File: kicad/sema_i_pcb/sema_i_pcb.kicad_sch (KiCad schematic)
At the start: 22 parts, among them SW1 SW_SPDT, SW2 SW_Push, U1 PIC24FJ64GA002-I_SP, U2 ESP8266-01_ESP-01, U3 edge_connector

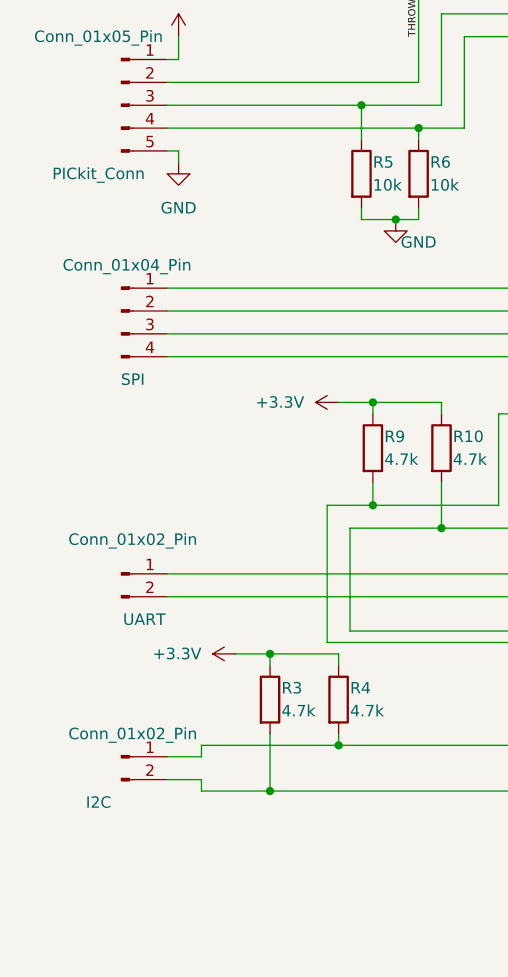
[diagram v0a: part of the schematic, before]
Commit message: Issue #9 : Kreiranje simbola i modela za Edge Connector
- Izmjenjen footprint edge connector-a
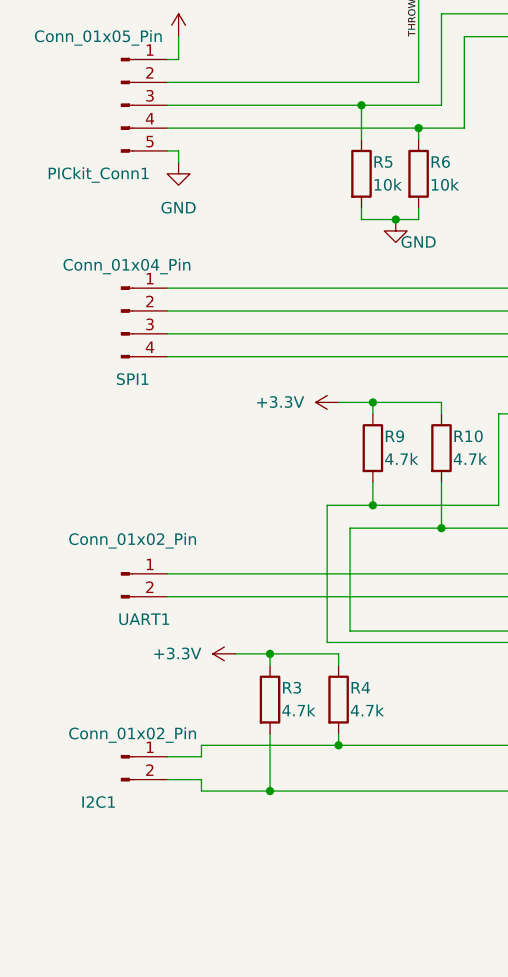
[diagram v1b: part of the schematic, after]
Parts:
- renumbered I2C to I2C1, PICkit_Conn to PICkit_Conn1, SPI to SPI1, UART to UART1
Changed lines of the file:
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@@
       (effects (font (size 1.27 1.27)) hide)
     )
+    (pin "1")
     (pin "10")
+    (pin "11")
+    (pin "12")
+    (pin "13")
+    (pin "14")
+    (pin "15")
+    (pin "16")
+    (pin "17")
+    (pin "18")
     (pin "19")
+    (pin "2")
+    (pin "20")
     (pin "21")
-    (pin "15")
+    (pin "22")
+    (pin "23")
     (pin "24")
-    (pin "13")
-    (pin "18")
-    (pin "11")
-    (pin "14")
+    (pin "25")
+    (pin "3")
+    (pin "4")
+    (pin "5")
+    (pin "6")
     (pin "7")
-    (pin "6")
     (pin "8")
-    (pin "16")
-    (pin "3")
-    (pin "12")
-    (pin "23")
-    (pin "2")
     (pin "9")
-    (pin "1")
-    (pin "25")
-    (pin "4")
-    (pin "22")
-    (pin "20")
-    (pin "17")
-    (pin "5")
     (instances
       (project "sema_i_pcb"
@@
   (symbol (lib_id "Connector:Conn_01x02_Pin") (at 24.13 132.08 0) (unit 1)
     (in_bom yes) (on_board yes) (dnp no)
-    (property "Reference" "UART" (at 26.67 137.16 0)
+    (property "Reference" "UART1" (at 26.67 137.16 0)
       (effects (font (size 1.27 1.27)))
     )
@@
       (project "sema_i_pcb"
         (path "/8dfcb1b3-4805-4434-ac9b-60b4afd3c281"
-          (reference "UART") (unit 1)
+          (reference "UART1") (unit 1)
         )
       )
@@
   (symbol (lib_id "Connector:Conn_01x04_Pin") (at 24.13 102.87 0) (unit 1)
     (in_bom yes) (on_board yes) (dnp no)
-    (property "Reference" "SPI" (at 25.4 110.49 0)
+    (property "Reference" "SPI1" (at 25.4 110.49 0)
       (effects (font (size 1.27 1.27)))
     )
@@
       (project "sema_i_pcb"
         (path "/8dfcb1b3-4805-4434-ac9b-60b4afd3c281"
-          (reference "SPI") (unit 1)
+          (reference "SPI1") (unit 1)
         )
       )
@@
   (symbol (lib_id "Connector:Conn_01x02_Pin") (at 24.13 152.4 0) (unit 1)
     (in_bom yes) (on_board yes) (dnp no)
-    (property "Reference" "I2C" (at 21.59 157.48 0)
+    (property "Reference" "I2C1" (at 21.59 157.48 0)
       (effects (font (size 1.27 1.27)))
     )
@@
       (project "sema_i_pcb"
         (path "/8dfcb1b3-4805-4434-ac9b-60b4afd3c281"
-          (reference "I2C") (unit 1)
+          (reference "I2C1") (unit 1)
         )
       )
@@
   (symbol (lib_id "Connector:Conn_01x05_Pin") (at 24.13 80.01 0) (unit 1)
     (in_bom yes) (on_board yes) (dnp no)
-    (property "Reference" "PICkit_Conn" (at 21.59 87.63 0)
+    (property "Reference" "PICkit_Conn1" (at 21.59 87.63 0)
       (effects (font (size 1.27 1.27)))
     )
@@
       (project "sema_i_pcb"
         (path "/8dfcb1b3-4805-4434-ac9b-60b4afd3c281"
-          (reference "PICkit_Conn") (unit 1)
-        )
-      )
+          (reference "PICkit_Conn1") (unit 1)
+        )
+      )

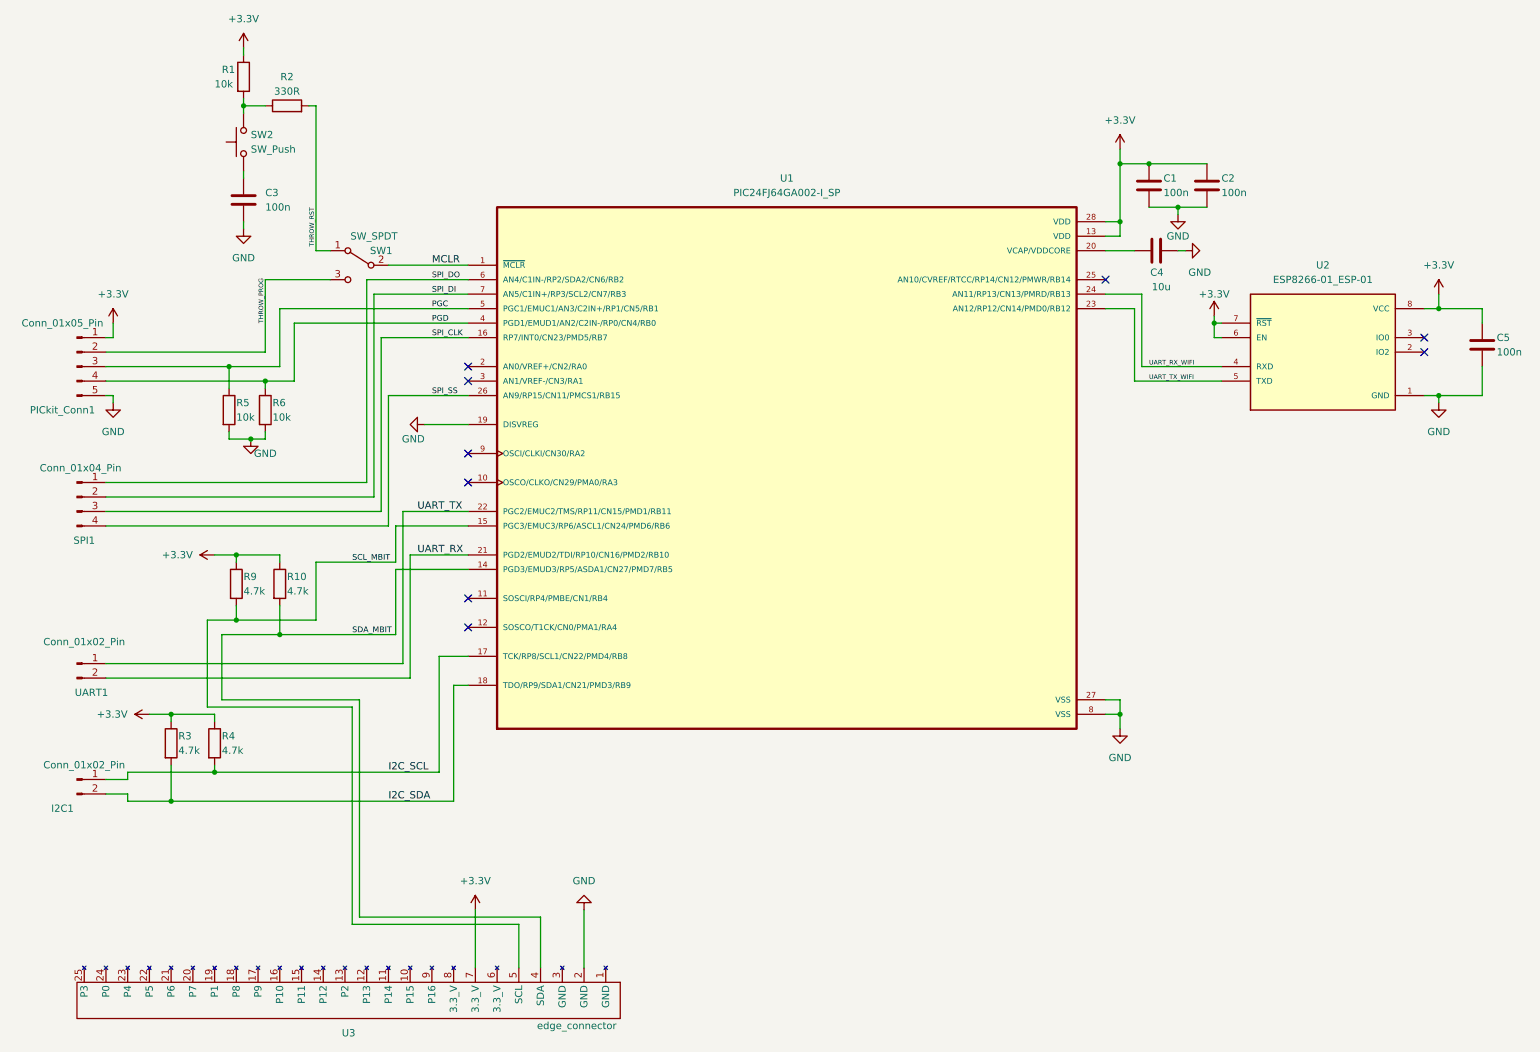
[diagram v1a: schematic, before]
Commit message: Issue #3 : Odabir komponenata štampane ploče
- Odabrane sve potrebne komponente
- Dodan .csv fajl sa komponentama i linkovima do kataloga
- Skupljeni svi otisci i modeli potrebni za PCB
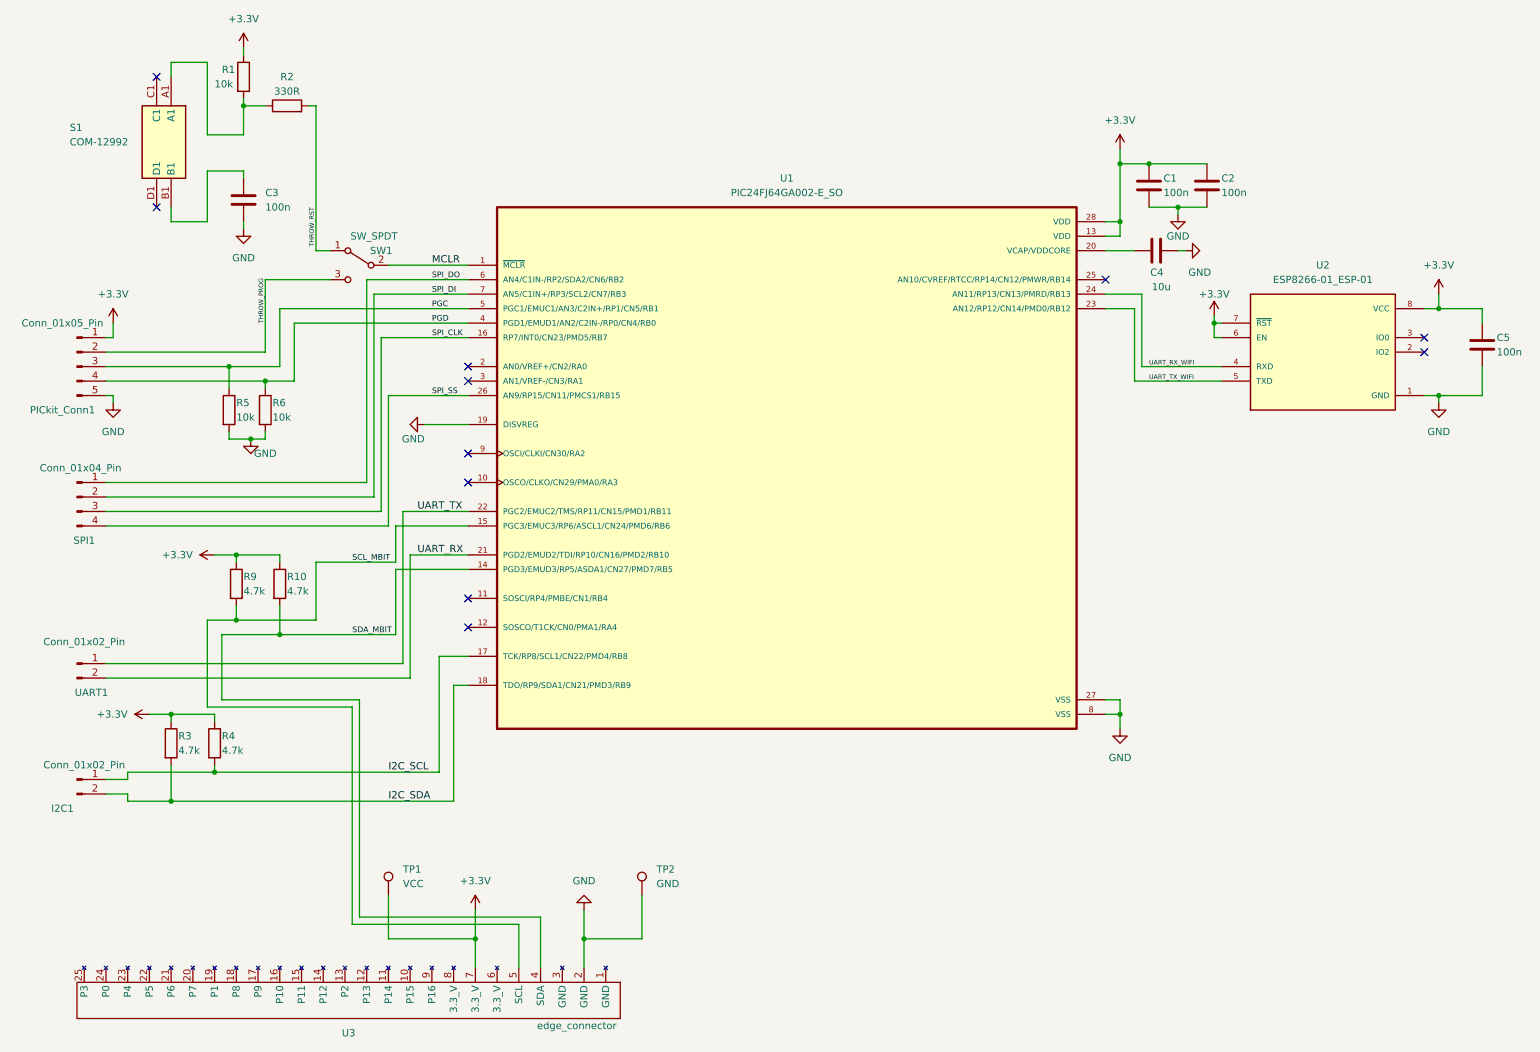
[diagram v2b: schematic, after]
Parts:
- removed SW2: SW_Push, Button_Switch_THT:SW_PUSH-12mm, symbol Switch:SW_Push
- added S1: COM-12992, COM12992, symbol PUSH_BTN:COM-12992
- added TP1: VCC, symbol Connector:TestPoint
- added TP2: GND, symbol Connector:TestPoint
- I2C1, UART1: footprint (none) -> PIN_HEADERS:HDRV2W70P0X254_1X2_478X244X884P
- PICkit_Conn1: footprint (none) -> PIN_HEADERS:HDRV5W56P0X254_1X5_1240X244X904P
- SPI1: footprint (none) -> PIN_HEADERS:A24PA254DSA71
- SW1: footprint (none) -> SPDT_SW:SLW12768644AD
- U1: value PIC24FJ64GA002-I_SP -> PIC24FJ64GA002-E_SO; footprint MCU:DIP787W46P254L3467H508Q28 -> MCU:SOIC28-W_MC_MCH
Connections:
- net +3.3V: now also TP1.1
- net GND: now also TP2.1
- net at C3.1: now also S1.B1
- net at R1.2, R2.1: now also S1.A1
- no-connect marks 9 -> 11

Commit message: Issue #3 : Odabir komponenata štampane ploče
- Promjenjen odabir za 10k i 4.7k otpornike
- Ažurirane promjene otisaka i modela u projektu
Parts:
- C1, C2, C3, C5: footprint (none) -> CAP_RES:100nF
- C4: footprint (none) -> CAP_RES:10uF
- R1, R5, R6: footprint (none) -> CAP_RES:10k
- R10, R3, R4, R9: footprint (none) -> CAP_RES:4k7
- R2: footprint (none) -> CAP_RES:330R
- S1: footprint COM12992 -> PUSH_BTN:COM12992
- SW1: footprint SPDT_SW:SLW12768644AD -> SW_SPDT:SLW12768644AD
- TP1, TP2: footprint (none) -> TestPoint:TestPoint_Pad_D2.0mm
- U3: footprint Connector:edge_connector -> EDGE_CONNECTOR:edge_connector
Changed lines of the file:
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@@
       (effects (font (size 1.27 1.27)))
     )
-    (property "Footprint" "Connector:edge_connector" (at 120.65 191.77 0)
+    (property "Footprint" "EDGE_CONNECTOR:edge_connector" (at 120.65 191.77 0)
       (effects (font (size 1.27 1.27)) hide)
     )
@@
       (effects (font (size 1.27 1.27)) (justify left))
     )
-    (property "Footprint" "" (at 54.3052 54.61 0)
+    (property "Footprint" "CAP_RES:100nF" (at 54.3052 54.61 0)
       (effects (font (size 1.27 1.27)) hide)
     )
@@
       (effects (font (size 1.27 1.27)) (justify left))
     )
-    (property "Footprint" "" (at 217.17 58.7248 0)
+    (property "Footprint" "CAP_RES:10uF" (at 217.17 58.7248 0)
       (effects (font (size 1.27 1.27)) hide)
     )
@@
       (effects (font (size 1.27 1.27)) (justify left))
     )
-    (property "Footprint" "" (at 51.562 29.21 90)
+    (property "Footprint" "CAP_RES:10k" (at 51.562 29.21 90)
       (effects (font (size 1.27 1.27)) hide)
     )
@@
       (effects (font (size 1.27 1.27)) (justify left))
     )
-    (property "Footprint" "" (at 213.0552 52.07 0)
+    (property "Footprint" "CAP_RES:100nF" (at 213.0552 52.07 0)
       (effects (font (size 1.27 1.27)) hide)
     )
@@
       (effects (font (size 1.27 1.27)) (justify left))
     )
-    (property "Footprint" "" (at 46.482 146.05 90)
+    (property "Footprint" "CAP_RES:4k7" (at 46.482 146.05 90)
       (effects (font (size 1.27 1.27)) hide)
     )
@@
       (effects (font (size 1.27 1.27)) (justify left))
     )
-    (property "Footprint" "" (at 50.292 118.11 90)
+    (property "Footprint" "CAP_RES:4k7" (at 50.292 118.11 90)
       (effects (font (size 1.27 1.27)) hide)
     )
@@
       (effects (font (size 1.27 1.27)) (justify left))
     )
-    (property "Footprint" "" (at 128.27 172.72 0)
+    (property "Footprint" "TestPoint:TestPoint_Pad_D2.0mm" (at 128.27 172.72 0)
       (effects (font (size 1.27 1.27)) hide)
     )
@@
       (effects (font (size 1.27 1.27)) (justify left))
     )
-    (property "Footprint" "" (at 55.372 87.63 90)
+    (property "Footprint" "CAP_RES:10k" (at 55.372 87.63 90)
       (effects (font (size 1.27 1.27)) hide)
     )
@@
       (effects (font (size 1.27 1.27)))
     )
-    (property "Footprint" "SPDT_SW:SLW12768644AD" (at 73.66 62.23 0)
+    (property "Footprint" "SW_SPDT:SLW12768644AD" (at 73.66 62.23 0)
       (effects (font (size 1.27 1.27)) hide)
     )
@@
       (effects (font (size 1.27 1.27)) (justify left))
     )
-    (property "Footprint" "" (at 57.912 118.11 90)
+    (property "Footprint" "CAP_RES:4k7" (at 57.912 118.11 90)
       (effects (font (size 1.27 1.27)) hide)
     )
@@
       (effects (font (size 1.27 1.27)) (justify left))
     )
-    (property "Footprint" "COM12992" (at -54.28 48.26 0)
+    (property "Footprint" "PUSH_BTN:COM12992" (at -54.28 48.26 0)
       (effects (font (size 1.27 1.27)) (justify left top) hide)
     )
@@
     )
     (pin "A1")
+    (pin "B1")
     (pin "C1")
     (pin "D1")
-    (pin "B1")
     (instances
       (project "sema_i_pcb"
@@
       (effects (font (size 1.27 1.27)) (justify left))
     )
-    (property "Footprint" "" (at 49.022 87.63 90)
+    (property "Footprint" "CAP_RES:10k" (at 49.022 87.63 90)
       (effects (font (size 1.27 1.27)) hide)
     )
@@
       (effects (font (size 1.27 1.27)) (justify left))
     )
-    (property "Footprint" "" (at 271.4752 80.01 0)
+    (property "Footprint" "CAP_RES:100nF" (at 271.4752 80.01 0)
       (effects (font (size 1.27 1.27)) hide)
     )
@@
       (effects (font (size 1.27 1.27)) (justify left))
     )
-    (property "Footprint" "" (at 223.2152 52.07 0)
+    (property "Footprint" "CAP_RES:100nF" (at 223.2152 52.07 0)
       (effects (font (size 1.27 1.27)) hide)
     )
@@
       (effects (font (size 1.27 1.27)))
     )
-    (property "Footprint" "" (at 60.96 36.068 90)
+    (property "Footprint" "CAP_RES:330R" (at 60.96 36.068 90)
       (effects (font (size 1.27 1.27)) hide)
     )
@@
       (effects (font (size 1.27 1.27)) (justify left))
     )
-    (property "Footprint" "" (at 83.82 172.72 0)
+    (property "Footprint" "TestPoint:TestPoint_Pad_D2.0mm" (at 83.82 172.72 0)
       (effects (font (size 1.27 1.27)) hide)
     )
@@
       (effects (font (size 1.27 1.27)) (justify left))
     )
-    (property "Footprint" "" (at 38.862 146.05 90)
-      (effects (font (size 1.27 1.27)) hide)
-    )
+    (property "Footprint" "CAP_RES:4k7" (at 38.862 146.05 90)
+      (effects (font (size 1.27 1.27)) hide)
+    )

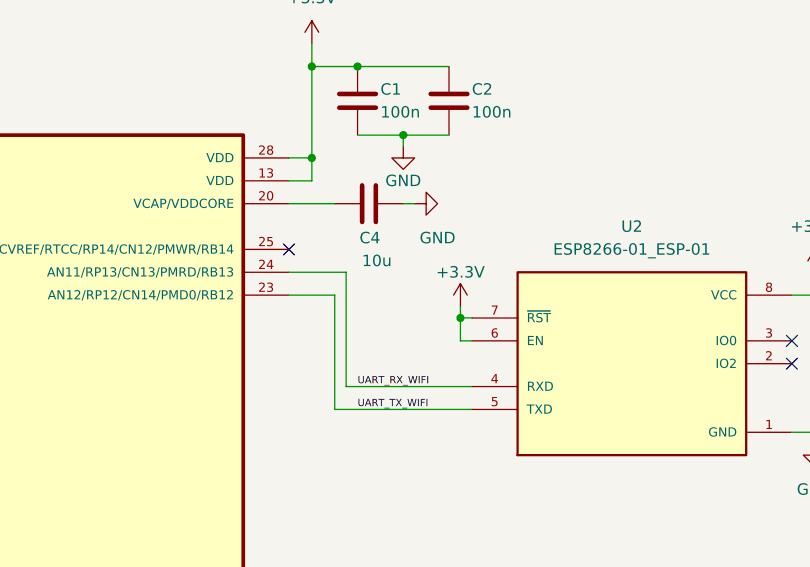
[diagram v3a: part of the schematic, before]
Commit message: Issue #4 : Projektovanje električne šeme
- Promjena na šemi, nakon dodatnog čitanja datasheet-a zaključeno je da RST pin WiFi modula mora biti pull-up otpornikom spojen na +3.3V umjesto direktno
- Novi otpornik dodat u .csv fajl
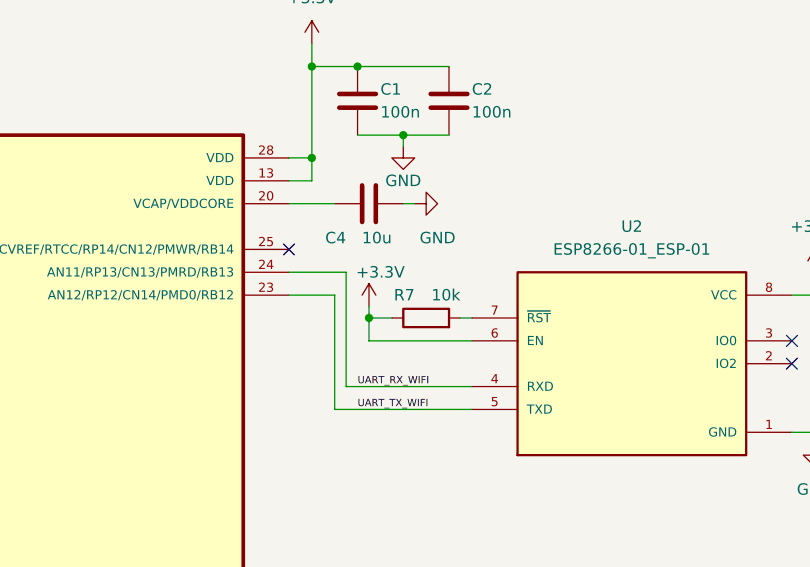
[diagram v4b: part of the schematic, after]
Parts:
- added R7: 10k, CAP_RES:10k, symbol Device:R
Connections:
- net +3.3V: now also R7.1; no longer U2.7 (~{RST})
- new net: R7.2, U2.7 (~{RST})

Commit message: Issue #7 : Raspored komponenata na PCB
- Dodana kompletirana šema , spremna za rutiranje.
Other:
- title: (none) -> Designed scheme autonomous vehicle
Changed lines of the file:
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@@
 (kicad_sch (version 20230121) (generator eeschema)
   (paper "A4")
+  (title_block
+    (title "Designed scheme autonomous vehicle")
+  )
   (junction (at 53.34 34.29) (diameter 0) (color 0 0 0 0)
   )
